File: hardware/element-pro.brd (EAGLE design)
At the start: 50.8 x 50.8 mm, 80 parts, among them J4 AMP FCI 10103594-0001LF, Q3 BSS138PW,115, Q4 BSS138PW,115, SW1 SPST_TACT-KMR2, U1 NEOPIXEL_NANO_2427, U10 TSL2591, U11 915MHz, U12 W25X40CLSNIG-ND-AT25F512BJEDE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, U14 SENSEAIR_S8, U15 VLP-450-F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

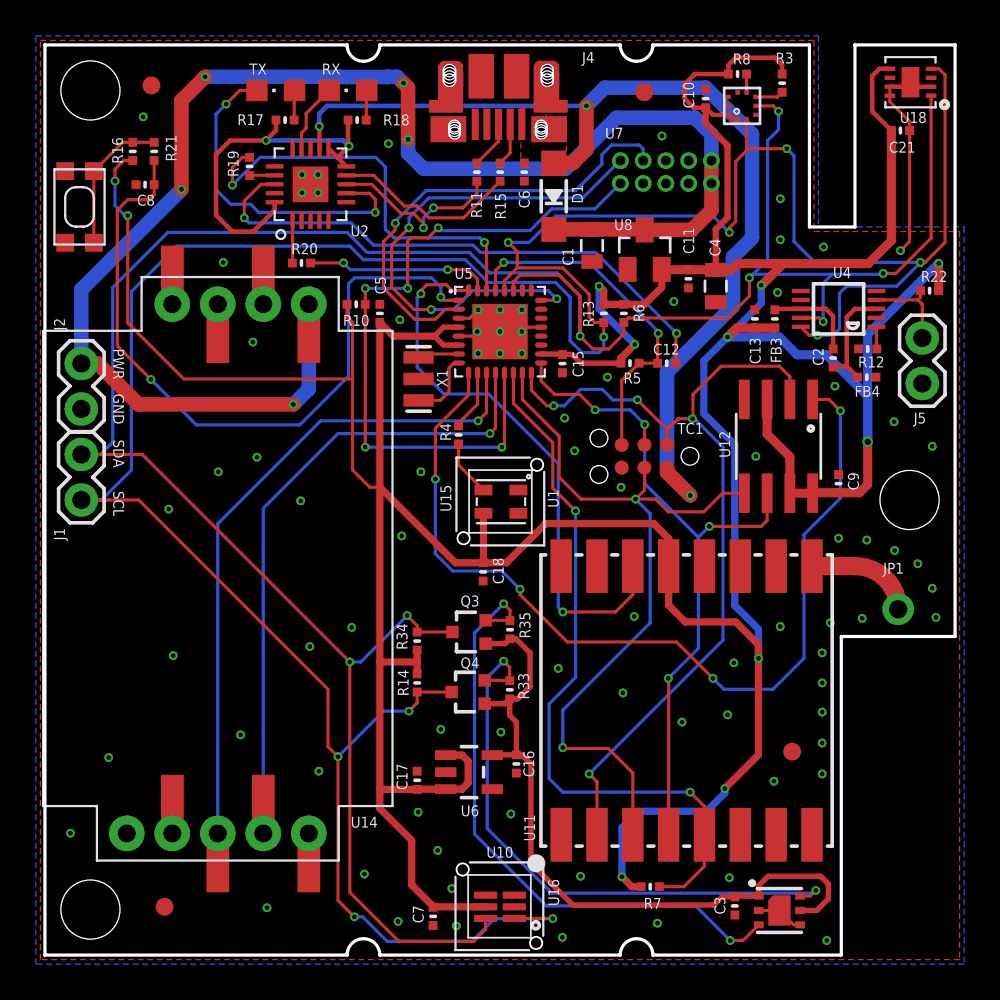
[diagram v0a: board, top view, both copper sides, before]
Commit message: silkscreen, nibbletz adjustment
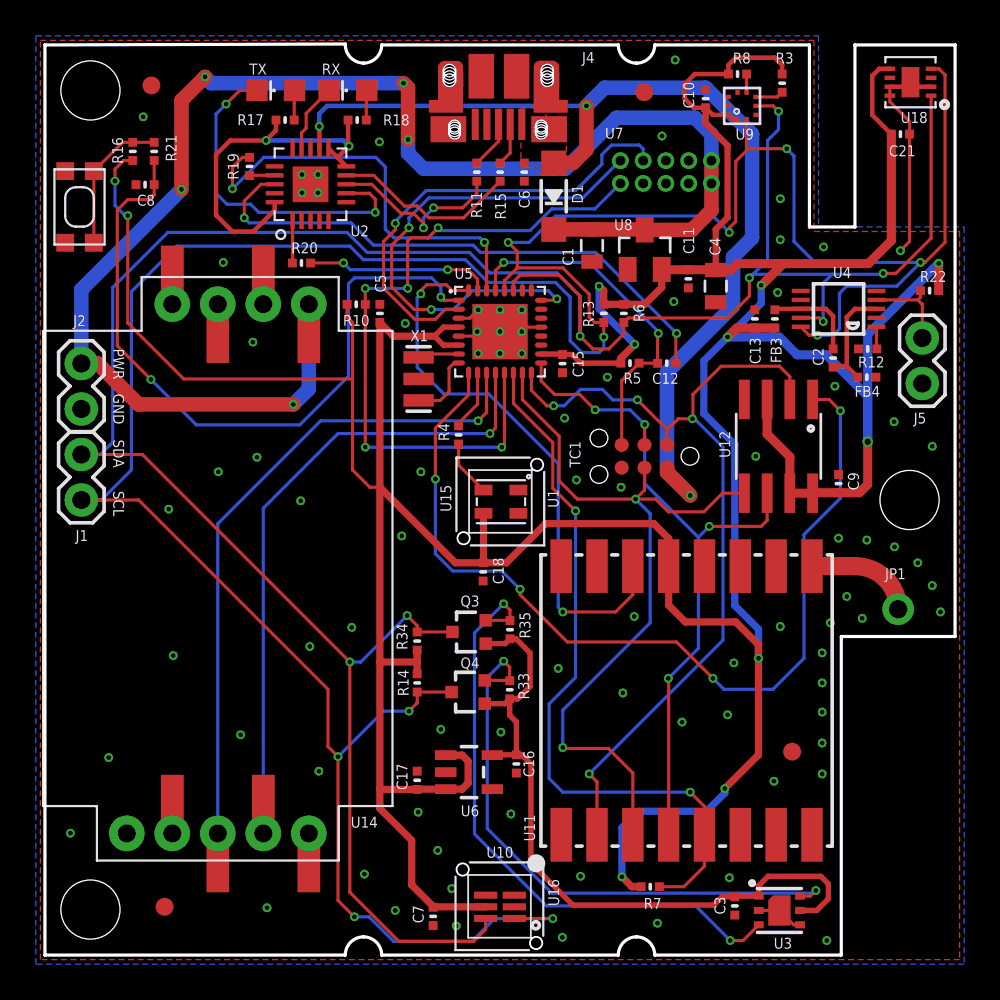
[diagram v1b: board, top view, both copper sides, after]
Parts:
- moved C21 0.20 mm to (47.8, 45.8)
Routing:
- net GND: vias 82 -> 84
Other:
- board size 50.8 x 50.8 mm -> 50.8 x 50.9 mm
- board text added: "U3"
- board text added: "U9"
